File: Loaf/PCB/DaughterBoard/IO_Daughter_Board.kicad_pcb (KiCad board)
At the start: 2 copper layers, 100 x 50 mm, 18 parts, among them J1 DB25_Socket, J2 Barrel Jack, J3 I/O Block, J4 5V Block, J5 Ground Block, J6 Ground Block, J7 Screw_Terminal_01x02, J8 Conn_01x02_Pin, SW1 SW_Push

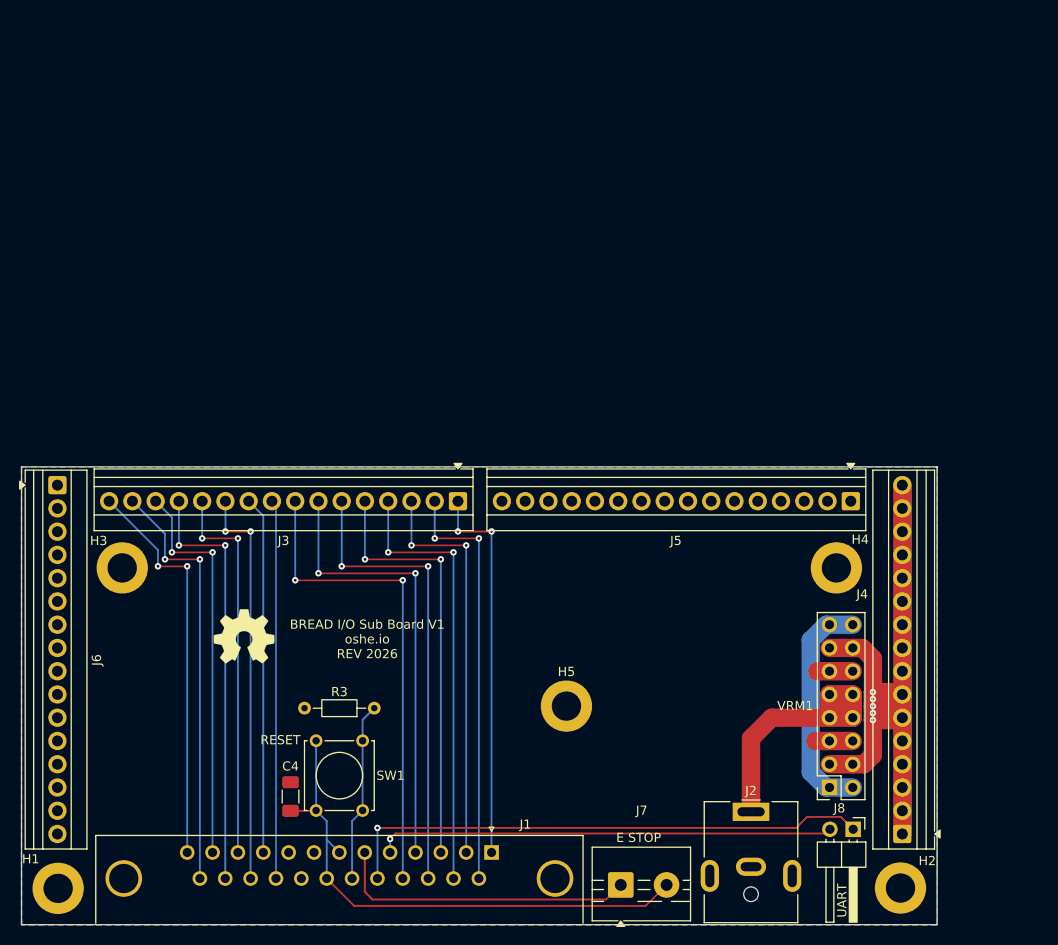
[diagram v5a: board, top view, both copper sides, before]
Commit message: Daughter board rework for purchasable terminals
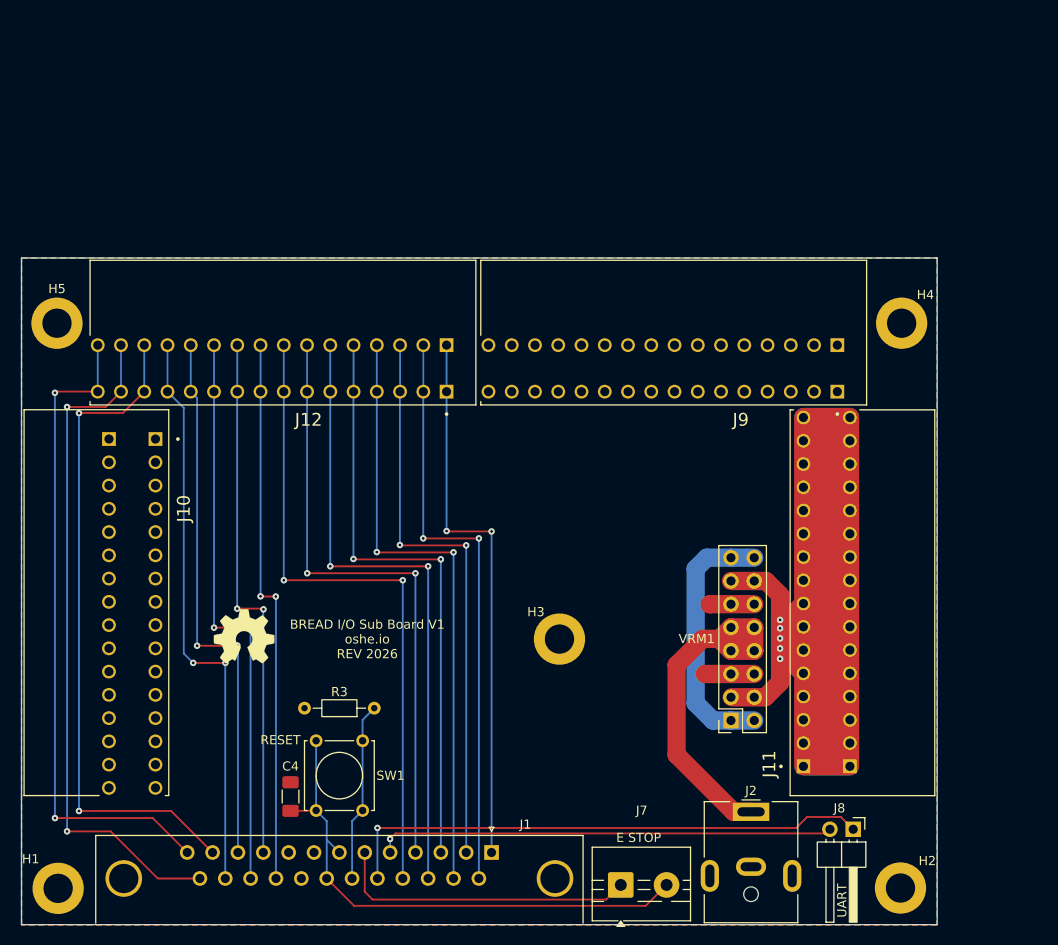
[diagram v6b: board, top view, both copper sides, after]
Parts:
- removed J3: I/O Block, TerminalBlock:TerminalBlock_Xinya_XY308-2.54-16P_1x16_P2.54mm_Horizontal
- removed J4: 5V Block, TerminalBlock:TerminalBlock_Xinya_XY308-2.54-16P_1x16_P2.54mm_Horizontal
- removed J5, J6: Ground Block, TerminalBlock:TerminalBlock_Xinya_XY308-2.54-16P_1x16_P2.54mm_Horizontal
- added J10: Ground Block 1, TBL009-254-16GY-2GY:CUI_TBL009-254-16GY-2GY, F.Cu at (96.6, 73.9)
- added J11: 5V Block, TBL009-254-16GY-2GY:CUI_TBL009-254-16GY-2GY, F.Cu at (167.4, 109.7)
- added J12: Logic Block, TBL009-254-16GY-2GY:CUI_TBL009-254-16GY-2GY, F.Cu at (128.4, 68.8)
- added J9: Ground Block 2, TBL009-254-16GY-2GY:CUI_TBL009-254-16GY-2GY, F.Cu at (171.1, 68.8)
- moved H5 69.6 mm to (85.9, 61.3)
- moved H3 48.4 mm to (140.8, 95.8)
- moved H4 27.7 mm to (178.1, 61.3)
- moved VRM1 13.0 mm to (159.5, 104.7)
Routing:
- net +5V: track 114.4 -> 82.1 mm
- net /AIO2: track 43.5 -> 73.1 mm
- net /AIO0: track 43.8 -> 72.3 mm
- net /AIO1: track 46.5 -> 74.7 mm
- net /AIO6: track 39.0 -> 58.3 mm, vias 0 -> 2
- net /AIO7: track 41.4 -> 59.9 mm, vias 0 -> 2
- net /DIO1: track 46.0 -> 64.3 mm
- net /DIO2: track 44.3 -> 62.6 mm
- net /AIO5: track 44.0 -> 62.3 mm
- net /DIO5: track 50.6 -> 68.9 mm
- net /DIO4: track 46.7 -> 64.9 mm
- net /DIO7: track 53.0 -> 71.2 mm
- net /DIO3: track 48.6 -> 66.9 mm
- net /DIO6: track 49.0 -> 67.2 mm
- net /DIO0: track 42.0 -> 60.3 mm
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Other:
- board size 100 x 50 mm -> 100 x 72.8 mm

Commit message: Added Gerbers
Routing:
- net +5V: track 82.1 -> 113.0 mm
